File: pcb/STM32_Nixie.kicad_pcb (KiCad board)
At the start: 4 copper layers, 184 parts, among them J1 CON_SAMTEC_14P_2R_1m27_P_KEY_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, J2 CONN_USBC_RCPT_USB2.0_USB4085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, Q1 NFET_250V_10A_TPH1110FNH,L1Q, Q2 NFET_60V_0A5_2N7002KT1G, SW1 ENC_SPST_24PPR_PEC12R-4225F-S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, U1 IC_SR_MC_HV5622PG-G, U2 IC_SR_MC_HV5622PG-G, U3 IC_MCU_STM32F100C4T6B_48LQFP, U4 IC_LVL_ONSEMI_MC14504BDTR2G, U5 REG_SW_BOOST_TI_TLV61046ADBV, U6 REG_SW_BOOST_TI_LM51561HPWPR, U7 REG_LDO_3V3_250mA_TI_LP5907MF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, U8 IC_FTDI_FT231XS, U9 IC_LSW_TI_TPS2552D, X1 XTAL_8M_20PPM_18pF_ECS-80-18-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, X2 XTAL_32K768_10PPM_7pF_ECS-.32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

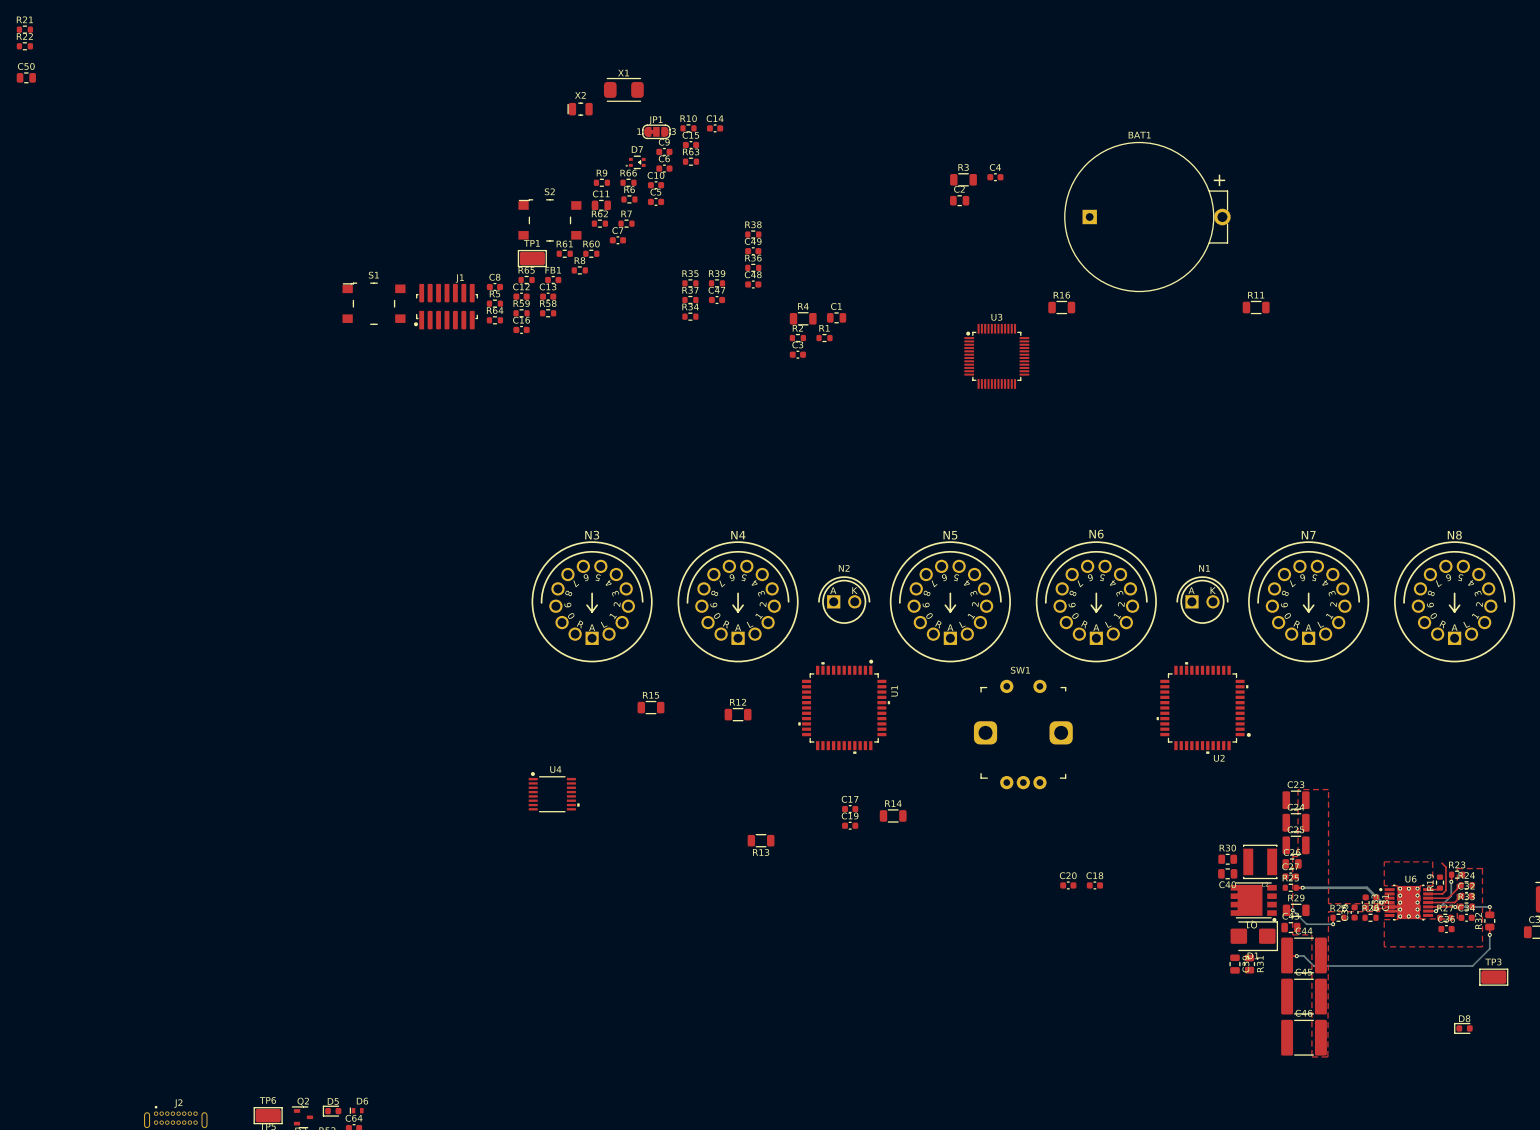
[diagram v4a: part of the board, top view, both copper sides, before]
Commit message: Added 180V clearance rules. Updated 0805 footprints to 1206 for 180V nets.
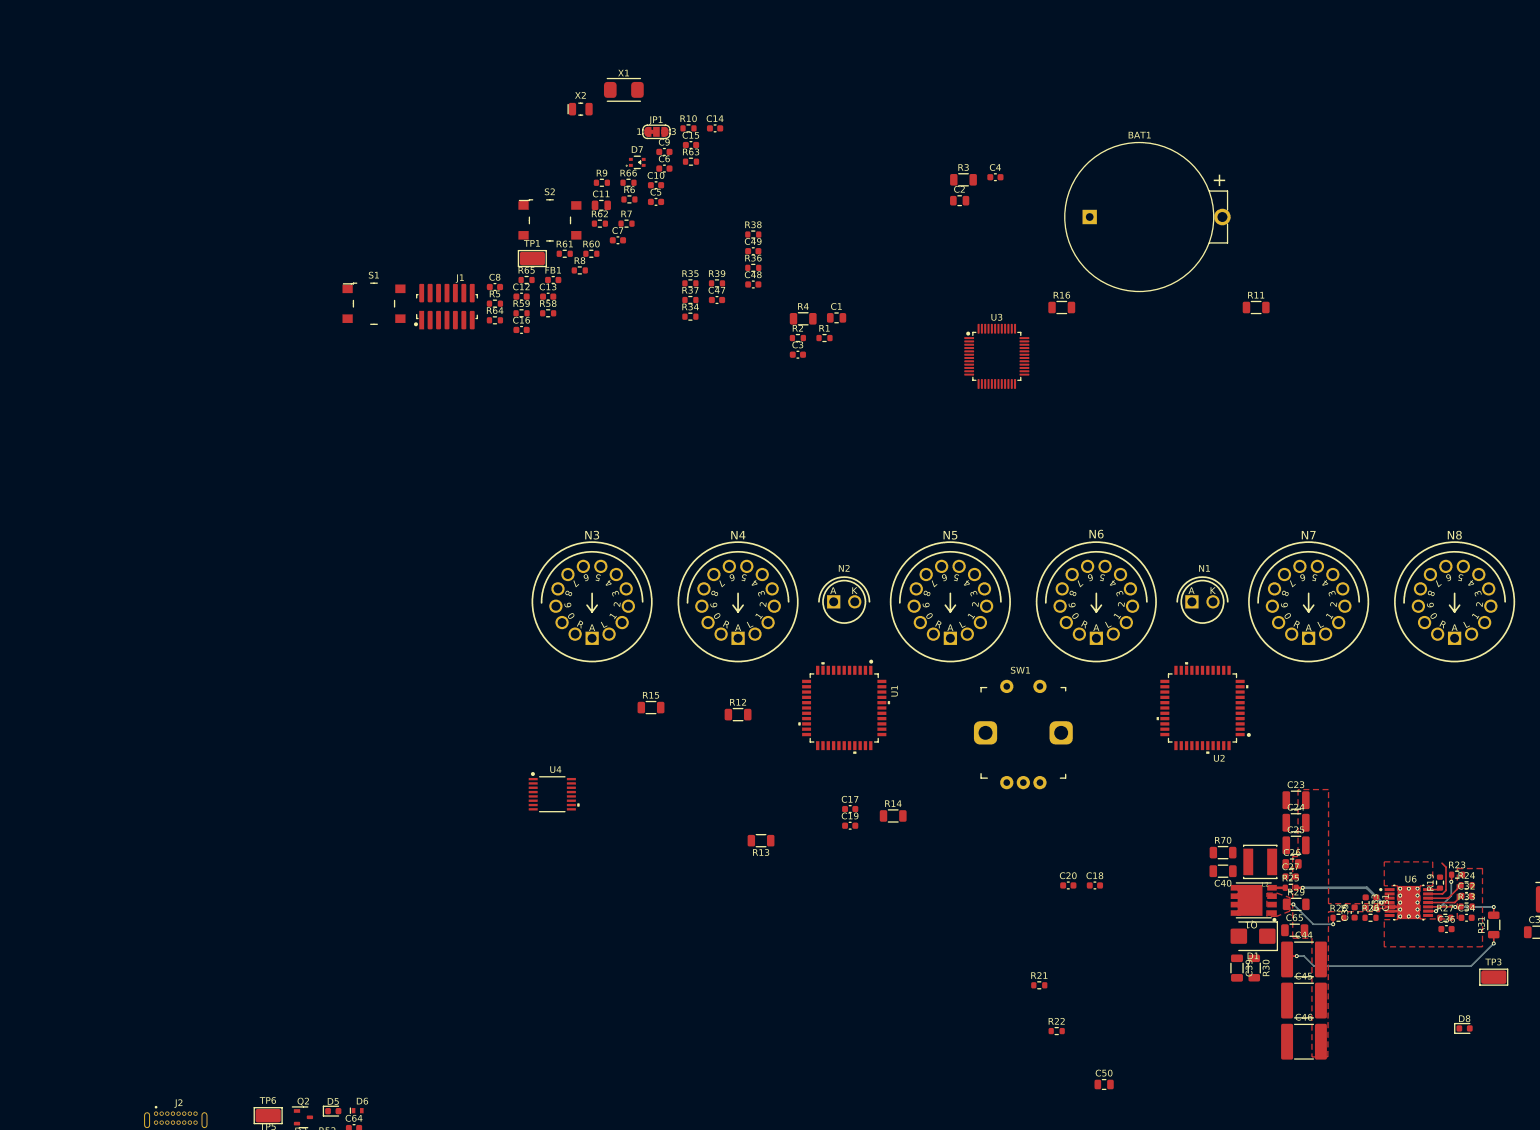
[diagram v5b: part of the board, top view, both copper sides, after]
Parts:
- removed C43: CAP_CER_0u1_250V_X7R_0805, Capacitor_SMD:C_0805_2012Metric
- removed R32: RES_499K_1P_1/4W_0805, Resistor_SMD:R_0805_2012Metric
- added C65: CAP_CER_0u1_250V_X7R_1206, Capacitor_SMD:C_1206_3216Metric, F.Cu at (192.9, 136.5)
- added R70: RES_DNP_1206, Resistor_SMD:R_1206_3216Metric, F.Cu at (182.1, 124.8)
- C39, C40: value CAP_CER_DNP_0805 -> CAP_CER_DNP_1206; footprint Capacitor_SMD:C_0805_2012Metric -> Capacitor_SMD:C_1206_3216Metric
- R30: value RES_DNP_0805 -> RES_DNP_1206; footprint Resistor_SMD:R_0805_2012Metric -> Resistor_SMD:R_1206_3216Metric
- R31: value RES_DNP_0805 -> RES_499K_1P_1/4W_1206; footprint Resistor_SMD:R_0805_2012Metric -> Resistor_SMD:R_1206_3216Metric
- moved C50 222.3 mm to (164.2, 159.8)
- moved R22 215.0 mm to (157.0, 151.7)
- moved R21 210.1 mm to (154.4, 144.8)
- moved R31 37.3 mm to (222.9, 135.7), turned to 90 degrees
- moved R30 16.9 mm to (186.8, 142.2), turned to -90 degrees
- moved R29 0.90 mm to (193.1, 132.6)
- moved C40 0.81 mm to (182.1, 127.6)
- moved C39 0.67 mm to (184.2, 142.2)
- moved C46 0.60 mm to (194.3, 153.3)
- moved C44 0.60 mm to (194.3, 140.9)
- moved C45 0.60 mm to (194.3, 147.1)
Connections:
- R30 pad 1: /Power/Q_SNUB -> 180V
- R30 pad 2: GND -> /Power/D_SNUB
- R31 pad 2: /Power/D_SNUB -> /Power/FB_180V
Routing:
- net /Power/GATE: track 0.00 -> 2.00 mm
- net 180V: track 35.6 -> 34.8 mm
- net /Power/FB_180V: track 11.4 -> 12.0 mm
- added copper zone on F.Cu, net /Power/CS_RAW

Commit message: Started mcu placement
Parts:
- added C43: CAP_CER_0u1_50V_X7R_0603, Capacitor_SMD:C_0603_1608Metric, F.Cu at (89.0, 51.4)
- moved R20 170.2 mm to (96.9, 65.3), turned to 90 degrees
- moved C54 169.4 mm to (93.5, 65.3), turned to -90 degrees
- moved C55 161.9 mm to (95.2, 65.3), turned to -90 degrees
- moved U3 53.3 mm to (95.0, 56.1)
- moved D8 49.5 mm to (268.0, 149.7)
- moved X1 49.1 mm to (79.7, 57.4), turned to -90 degrees
- moved R10 48.9 mm to (84.7, 61.6)
- moved C14 47.1 mm to (98.2, 62.2), turned to 180 degrees
- moved R9 46.4 mm to (112.2, 63.7)
- moved R38 45.5 mm to (83.5, 67.7), turned to -90 degrees
- moved C15 43.8 mm to (87.8, 59.6), turned to 180 degrees
- moved R5 43.2 mm to (112.2, 58.7)
- moved C10 40.9 mm to (84.7, 63.3), turned to 180 degrees
- moved C49 38.7 mm to (88.2, 65.2)
- moved X2 38.3 mm to (84.9, 51.0), turned to 180 degrees
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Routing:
- net /MCU/OSC_IN: track 0.00 -> 12.2 mm
- net /MCU/OSC32_IN: track 0.00 -> 7.82 mm
- net /MCU/OSC_OUT: track 0.00 -> 7.50 mm
- net /MCU/OSC_OUT_R: track 0.00 -> 5.77 mm
- net /MCU/OSC32_OUT: track 0.00 -> 4.93 mm
- net /MCU/OSC32_OUT_R: track 0.00 -> 4.16 mm
- net /Power/CS_RAW: track 9.27 -> 6.01 mm
- net 180V: track 34.8 -> 31.5 mm
- net /Power/GATE_R: track 15.0 -> 12.6 mm
- added copper zone on F.Cu, net /Power/SW_180V

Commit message: Placement V1. Want to try and centre the board on the nixies vertically. Saving progress before trying out different placements.
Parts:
- BAT1: moved to B.Cu
- moved U9 148.1 mm to (167.6, 122.9)
- moved R57 143.2 mm to (165.3, 128.8)
- moved R54 142.5 mm to (170.6, 124.2), turned to -90 degrees
- moved TP6 142.5 mm to (173.9, 121.0)
- moved R40 140.2 mm to (159.0, 127.5)
- moved R53 140.1 mm to (165.3, 127.1), turned to 180 degrees
- moved R69 138.8 mm to (128.9, 129.4), turned to 90 degrees
- moved R56 138.7 mm to (173.7, 129.7)
- moved FB5 136.5 mm to (158.1, 125.5)
- moved Q2 135.5 mm to (173.7, 127.0), turned to 90 degrees
- moved R55 134.7 mm to (172.2, 124.2), turned to -90 degrees
- moved J2 133.0 mm to (152.0, 131.7)
- moved D10 132.7 mm to (127.1, 129.4), turned to 90 degrees
- moved TP5 131.2 mm to (161.5, 123.5), turned to 90 degrees
- moved C53 130.5 mm to (158.1, 121.9), turned to 180 degrees
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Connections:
- net Net-(D7-BK) renamed /MCU/LED_BLUE_R
- net Net-(D7-GK) renamed /MCU/LED_GREEN_R
- net Net-(D7-RK) renamed /MCU/LED_RED_R
- net Net-(J2-CC1) renamed /USB Connector/CC1
- net Net-(J2-CC2) renamed /USB Connector/CC2
- net Net-(Q2-D) renamed /USB Connector/ILIM2
- net Net-(R5-Pad1) renamed /MCU/BOOT0_SW
- net Net-(U9-ILIM) renamed /USB Connector/ILIM_5V_LS
- R1 pad 2: /Nixie Display/nPOL_12V -> /nPOL_12V
- U1 pad 27: /Nixie Display/nPOL_12V -> /nPOL_12V
- U2 pad 33: /Nixie Display/nPOL_12V -> /nPOL_12V
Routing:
- net /MCU/PG_180V: track 7.27 -> 2.21 mm, vias 0 -> 1
- net /MCU/EN_180V: track 1.93 -> 3.03 mm, vias 0 -> 1

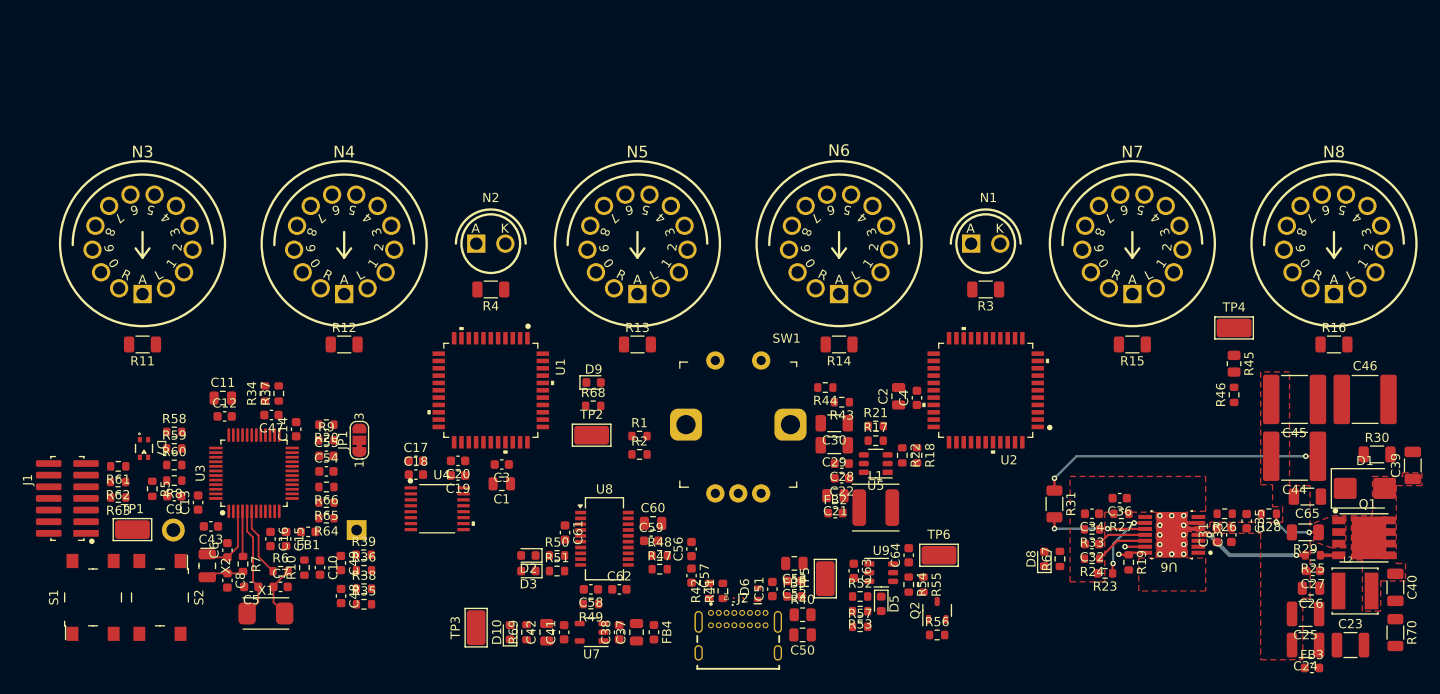
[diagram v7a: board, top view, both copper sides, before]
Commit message: Liking this placement a lot better -- board is looking more symmetric north to south
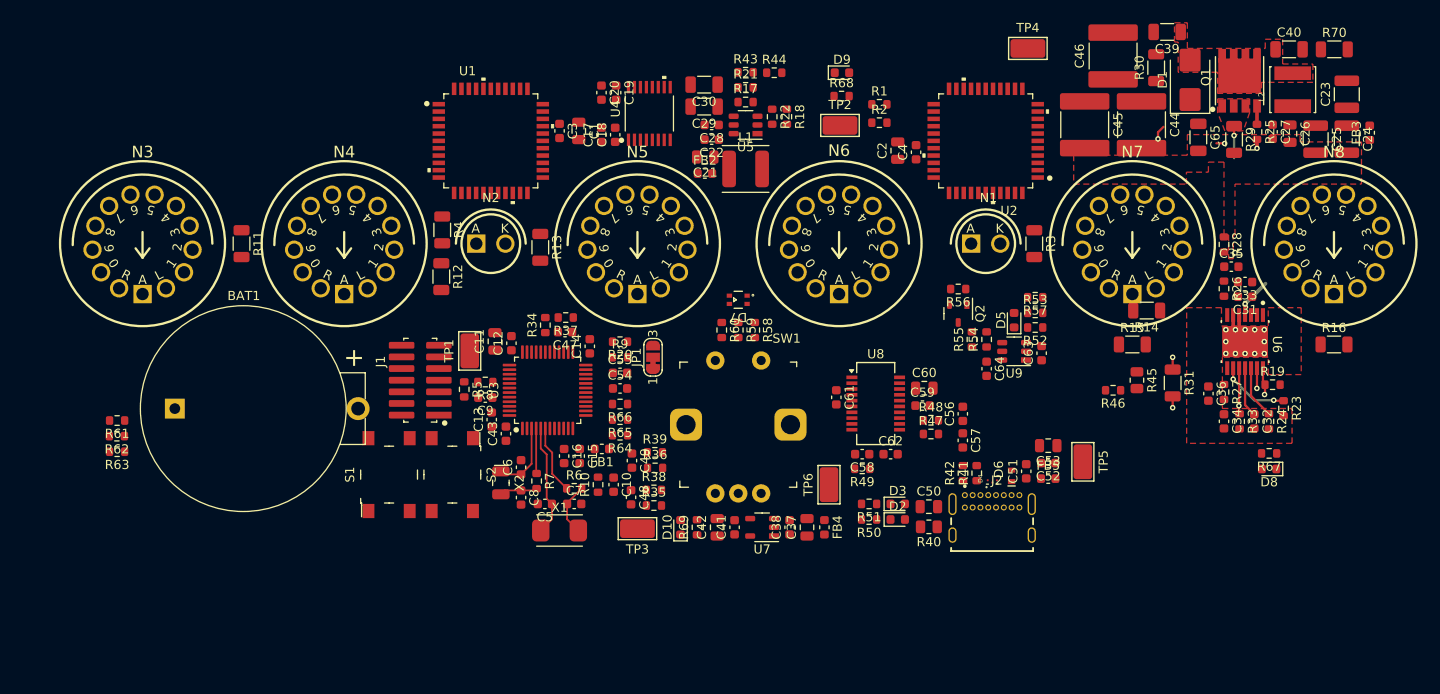
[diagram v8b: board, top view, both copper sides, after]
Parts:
- BAT1: moved to F.Cu
- moved D7 66.8 mm to (152.0, 93.1), turned to 180 degrees
- moved R58 64.3 mm to (153.8, 96.4), turned to -90 degrees
- moved R70 64.0 mm to (217.0, 65.8), turned to 0 degrees
- moved R59 62.9 mm to (152.0, 96.4), turned to -90 degrees
- moved R60 61.5 mm to (150.2, 96.4), turned to -90 degrees
- moved C23 60.1 mm to (218.4, 70.7), turned to 90 degrees
- moved C40 59.8 mm to (212.1, 65.8), turned to 0 degrees
- moved FB3 58.7 mm to (220.9, 74.9), turned to 90 degrees
- moved C24 55.4 mm to (218.4, 75.6), turned to -90 degrees
- moved L2 55.1 mm to (212.5, 70.2), turned to 90 degrees
- moved C39 54.4 mm to (198.8, 63.9), turned to 180 degrees
- moved C25 51.8 mm to (215.0, 75.6), turned to -90 degrees
- moved Q1 51.7 mm to (206.7, 69.2), turned to 90 degrees
- moved C26 49.7 mm to (212.2, 75.0), turned to -90 degrees
- moved U4 48.9 mm to (142.3, 72.8), turned to 90 degrees
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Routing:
- net 180V: track 31.5 -> 1.54 mm, vias 2 -> 1
- net /Power/GATE_R: track 12.6 -> 5.32 mm
- net /Power/FB_180V: track 12.0 -> 6.20 mm
- net /Power/CS_RAW: track 6.01 -> 3.51 mm, vias 2 -> 1
- net GND: track 6.71 -> 9.20 mm, vias 12 -> 14
